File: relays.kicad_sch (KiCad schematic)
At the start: 1 part, among them J10 Conn_01x26_Pin

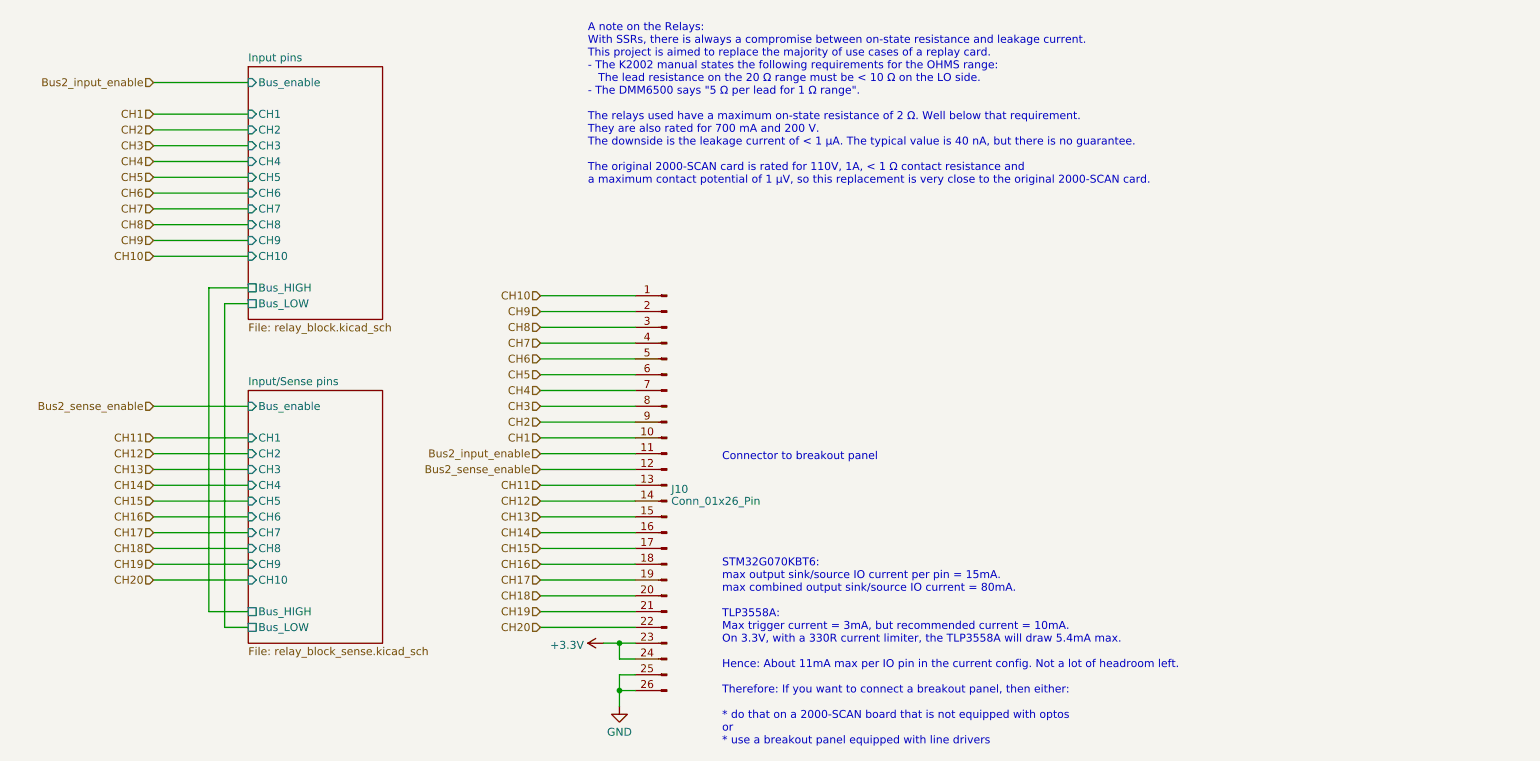
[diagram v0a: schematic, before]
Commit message: Version 1.6
Created a high-voltage rated scan board.

Control is done completely in logic to avoid programming an MCU
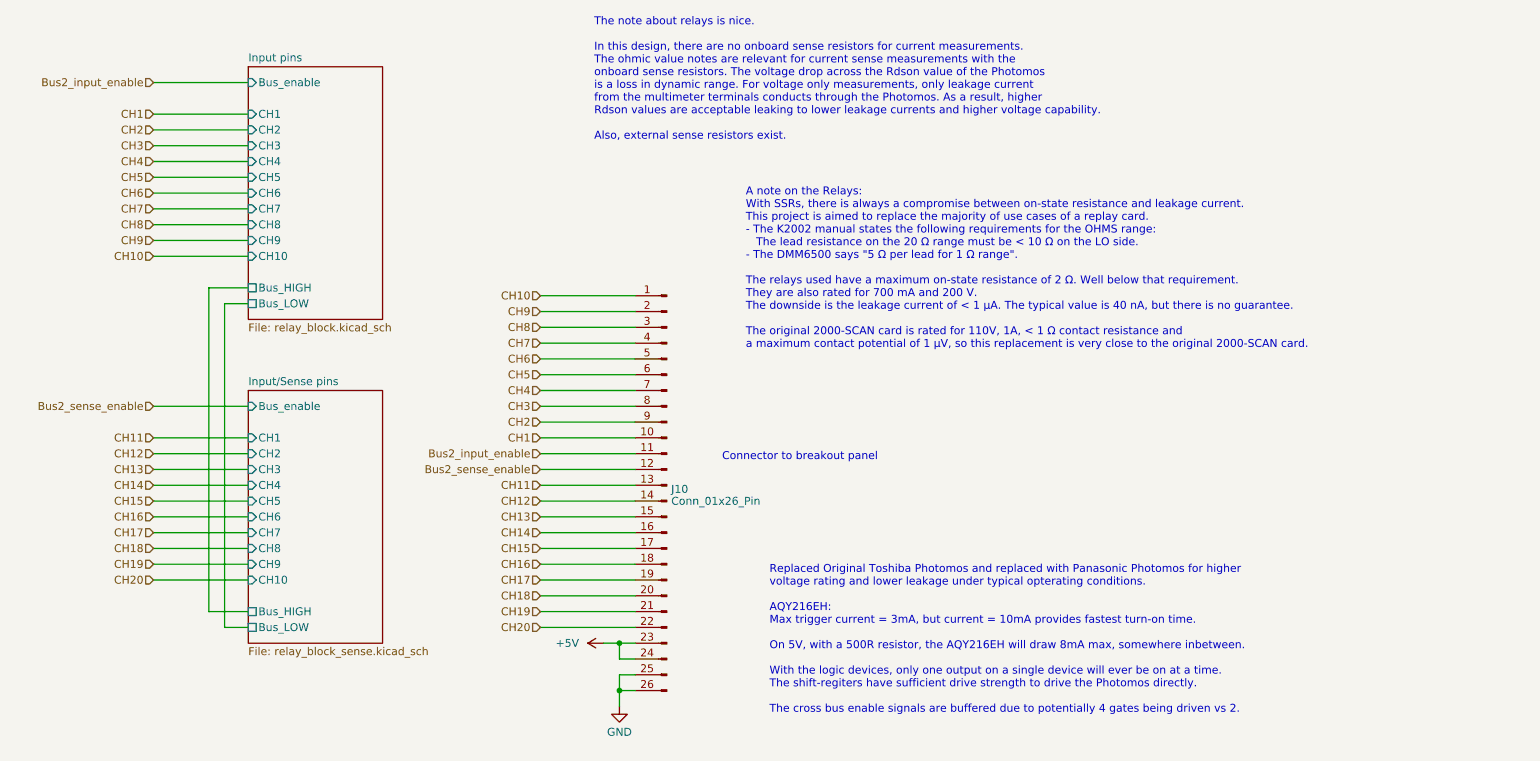
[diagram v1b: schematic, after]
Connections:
- net +3.3V renamed +5V
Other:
- note added: "Replaced Original Toshiba Photomos and replaced with Panasonic Photomos for higher voltage rating and lower leakage under typical opterating conditions. AQY216EH: Max trigger current = 3mA, but current = 10mA provides fastest turn-on time. On 5V, with a 500R resistor, the AQY216EH will draw 8mA max, somewhere inbetween. With the logic devices, only one output on a single device will ever be on at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"
- note added: "The note about relays is nice. In this design, there are no onboard sense resistors for current measurements. The ohmic value notes are relevant for current sense measurements with the onboard sense resistors. The voltage drop across the Rdson value of the Photomos is a loss in dynamic range. For voltage only measurements, only leakage current from the multimeter terminals conducts through the Ph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"
- note removed: "STM32G070KBT6: max output sink/source IO current per pin = 15mA. max combined output sink/source IO current = 80mA. TLP3558A: Max trigger current = 3mA, but recommended current = 10mA. On 3.3V, with a 330R current limiter, the TLP3558A will draw 5.4mA max. Hence: About 11mA max per IO pin in the current config. Not a lot of headroom left. Therefore: If you want to connect a breakout panel, then e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"
